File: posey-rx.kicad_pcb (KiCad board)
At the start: 6 copper layers, 25 x 12.5 mm, 31 parts, among them J1 TC2050-IDC-NL, Y1 XTAL, Y2 XTAL

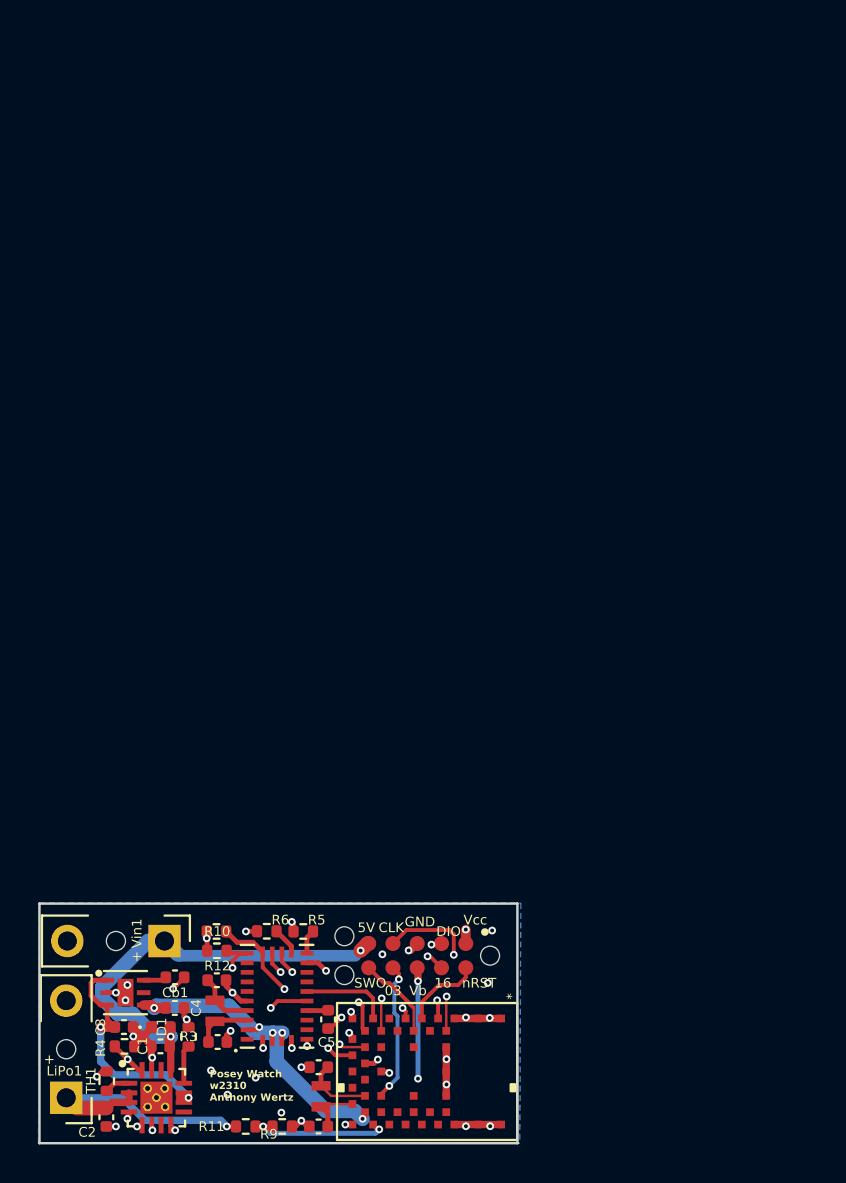
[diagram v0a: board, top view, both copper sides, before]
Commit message: Updated readme, license, and version.
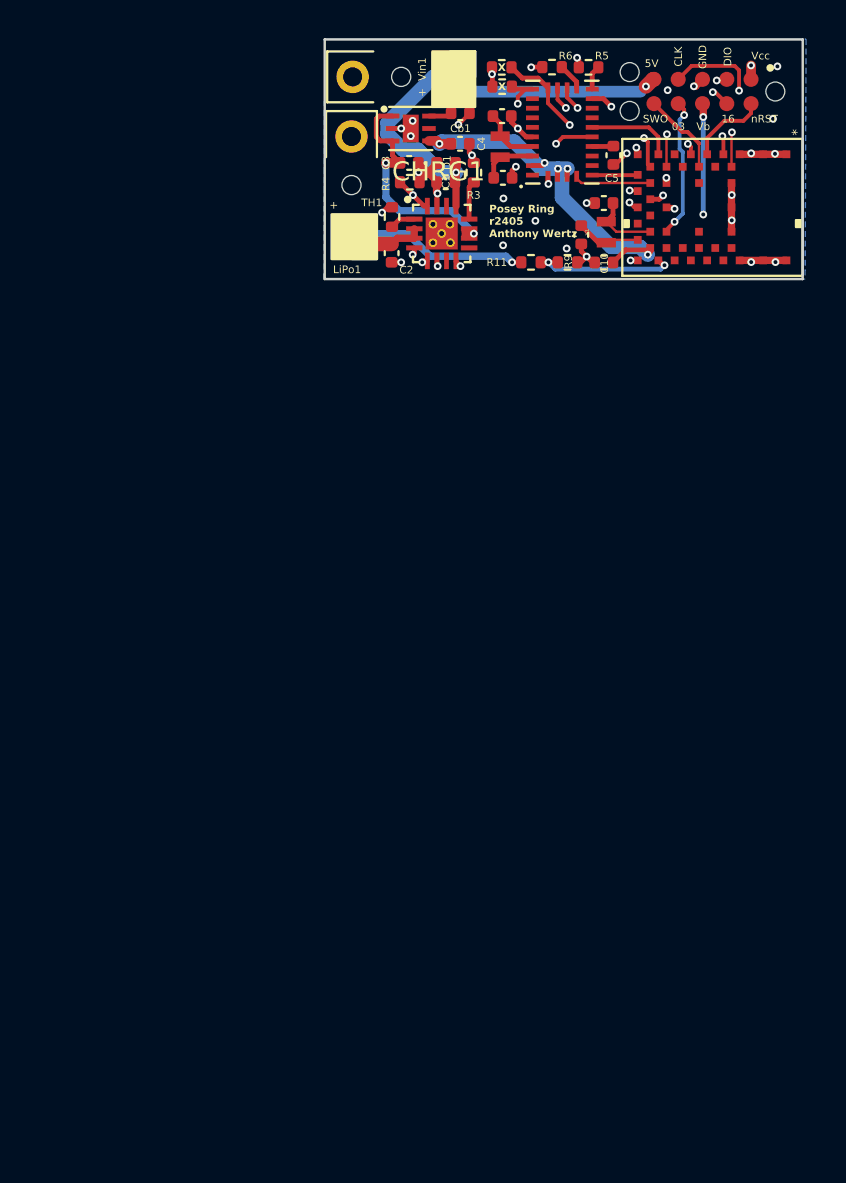
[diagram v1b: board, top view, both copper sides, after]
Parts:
- added C10: 0.1µ, Capacitor_SMD:C_0402_1005Metric, F.Cu at (150.5, 98.5)
- D1: value D_TVS -> ACPDQC5V0R-HF
- IMU1: value BNO080 -> BNO086
- TH1: value NTC -> 10k
- Y1, Y2: value XTAL -> ECS-.327-9-16-TR
- moved C8 48.6 mm to (149.3, 97.1), turned to 90 degrees
- moved TH1 47.6 mm to (139.4, 96.1)
- moved C2 47.6 mm to (139.4, 98.0)
- moved C4 47.6 mm to (143.0, 92.3)
- moved C6 47.6 mm to (145.2, 94.1)
- moved CHRG1 47.6 mm to (142.0, 97.0)
- moved Cb1 47.6 mm to (143.0, 90.7)
- moved G*** 47.6 mm to (149.2, 95.0)
- moved R10 47.6 mm to (145.2, 88.3)
- moved R5 47.6 mm to (149.7, 88.3)
- moved R6 47.6 mm to (147.8, 88.3)
- moved Y1 47.6 mm to (150.6, 96.9)
- moved C3 47.6 mm to (140.3, 93.3)
- moved Vin1 47.6 mm to (142.5, 88.8)
- moved C1 47.6 mm to (142.3, 94.3)
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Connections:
- IMU1 pad 5: GND -> IMU_PS1
- IMU1 pad 6: GND -> IMU_PS0
- µC1 pad 16: SPI_CS_IMU -> IMU_PS0
- µC1 pad 17: SCL/SPI_SCK -> IMU_PS1
- µC1 pad 18: SDA/SPI_CIPO -> SCL/SPI_SCK
- µC1 pad 20: unconnected-(µC1A-P0-08-Pad20) -> SDA/SPI_CIPO
- µC1 pad 42: unconnected-(µC1A-P0-19-Pad42) -> SPI_CS_IMU
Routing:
- net IMU_PS1: track 0.00 -> 4.05 mm
- net IMU_PS0: track 0.00 -> 2.39 mm
- net VCC: track 40.7 -> 42.5 mm
- net SPI_CS_IMU: track 6.53 -> 8.27 mm
- net I_CHG: track 16.3 -> 17.4 mm
- net Net-(µC1A-P0-00/XTAL1): track 2.88 -> 3.39 mm
- net GND: vias 38 -> 36
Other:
- board text added: "Posey Ring r2405 Anthony Wertz"
- board text added: "X"
- board text removed: "Posey Watch w2310 Anthony Wertz"
